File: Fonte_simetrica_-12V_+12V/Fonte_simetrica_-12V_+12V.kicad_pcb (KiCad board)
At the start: 2 copper layers, 23 parts, among them Q1 AO3401A, U1 TPS65131RGER

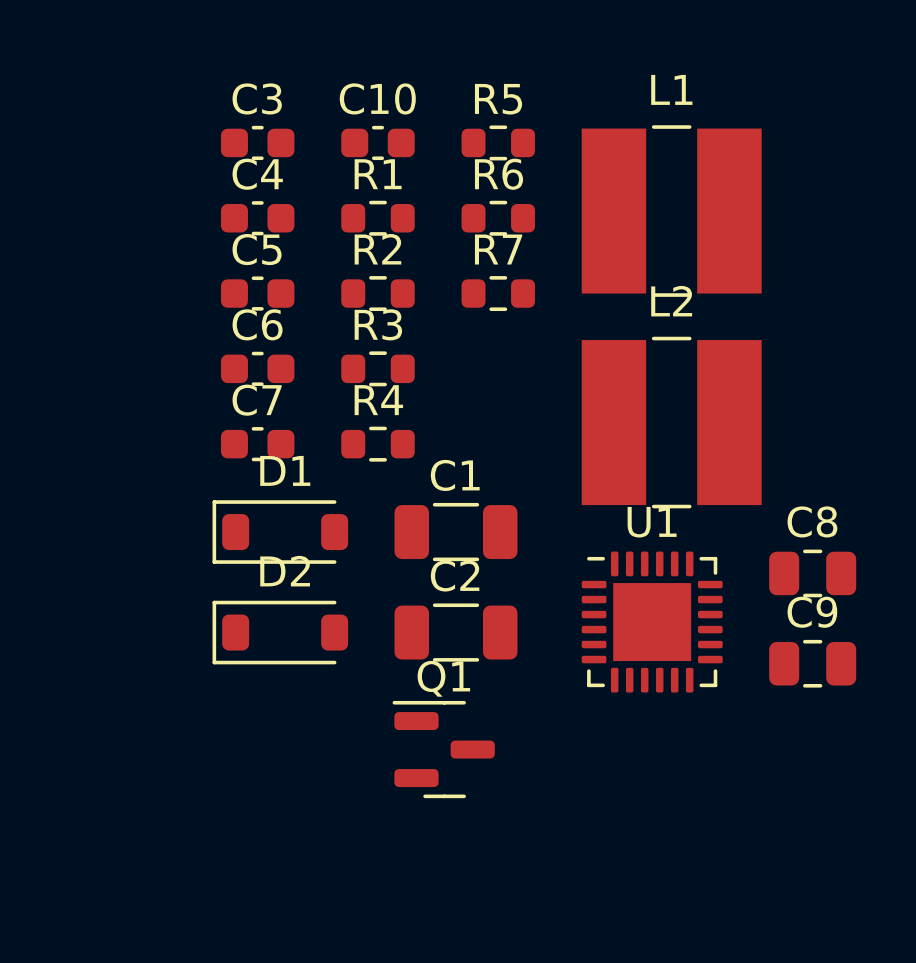
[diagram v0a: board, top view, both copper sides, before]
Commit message: add power 12+ and 12-
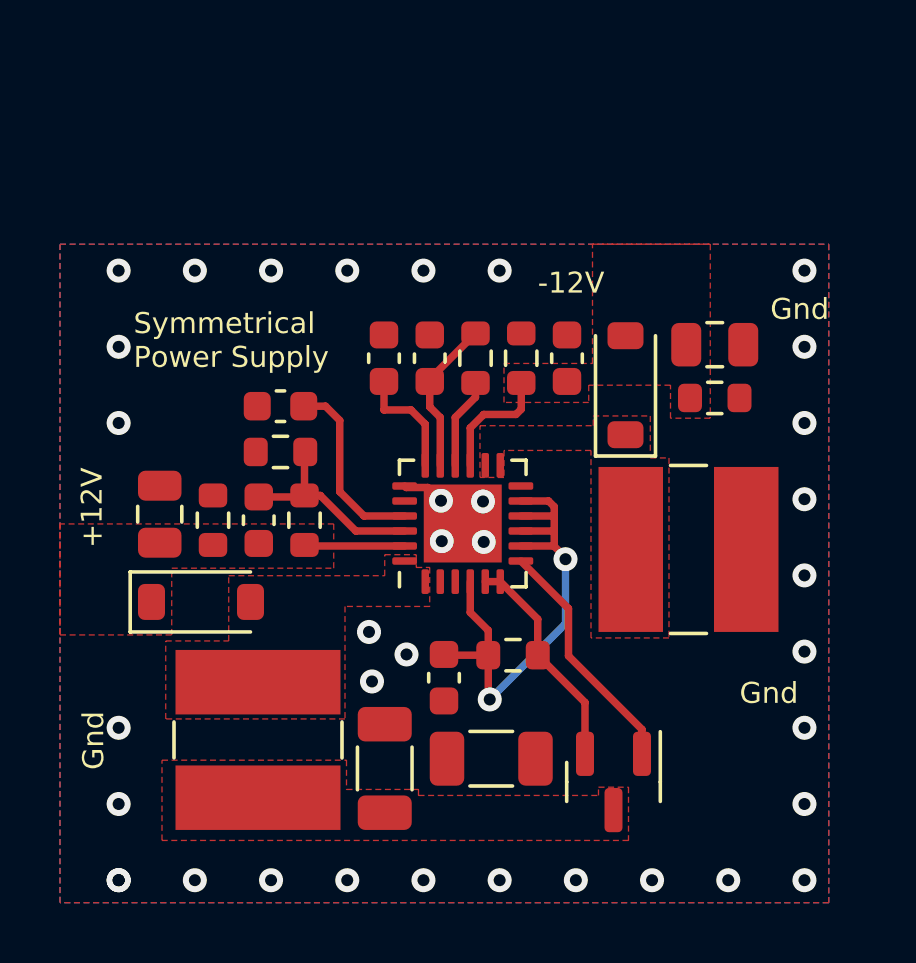
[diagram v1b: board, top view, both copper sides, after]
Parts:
- removed C1, C2: 10u, Capacitor_SMD:C_1206_3216Metric
- removed C10: 4n7, Capacitor_SMD:C_0603_1608Metric
- removed C3: 100n, Capacitor_SMD:C_0603_1608Metric
- removed C4: 10n, Capacitor_SMD:C_0603_1608Metric
- removed C5: 6p8, Capacitor_SMD:C_0603_1608Metric
- removed C6: 8p2, Capacitor_SMD:C_0603_1608Metric
- removed C7: 220n, Capacitor_SMD:C_0603_1608Metric
- removed C8, C9: 22u, Capacitor_SMD:C_0805_2012Metric
- removed D1, D2: B5819W, Diode_SMD:D_SOD-123
- removed L1, L2: 10u, Inductor_SMD:L_TracoPower_TCK-047_5.2x5.8mm
- removed Q1: AO3401A, Package_TO_SOT_SMD:SOT-23
- removed R1: 100, Resistor_SMD:R_0603_1608Metric
- removed R2, R5: 1M, Resistor_SMD:R_0603_1608Metric
- removed R3: 110k, Resistor_SMD:R_0603_1608Metric
- removed R4: 100k, Resistor_SMD:R_0603_1608Metric
- removed R6, R7: 12k, Resistor_SMD:R_0603_1608Metric
- removed U1: TPS65131RGER, Package_DFN_QFN:QFN-24-1EP_4x4mm_P0.5mm_EP2.6x2.6mm
- added CFS1: 10u, Capacitor_SMD:C_1206_3216Metric, F.Cu at (142.1, 82.0)
- added CFS10: 4n7, Capacitor_SMD:C_0603_1608Metric, F.Cu at (138.6, 68.6)
- added CFS2: 10u, Capacitor_SMD:C_1206_3216Metric, F.Cu at (138.6, 82.3)
- added CFS3: 100n, Capacitor_SMD:C_0603_1608Metric, F.Cu at (140.6, 79.3)
- added CFS4: 10n, Capacitor_SMD:C_0603_1608Metric, F.Cu at (135.1, 70.2)
- added CFS5: 6p8, Capacitor_SMD:C_0603_1608Metric, F.Cu at (134.4, 74.0)
- added CFS6: 8p2, Capacitor_SMD:C_0603_1608Metric, F.Cu at (144.7, 68.6)
- added CFS7: 220n, Capacitor_SMD:C_0603_1608Metric, F.Cu at (140.1, 68.6)
- added CFS8: 22u, Capacitor_SMD:C_0805_2012Metric, F.Cu at (149.6, 68.2)
- added CFS9: 22u, Capacitor_SMD:C_0805_2012Metric, F.Cu at (131.1, 73.8)
- added DFS1: B5819W, Diode_SMD:D_SOD-123, F.Cu at (132.4, 76.8)
- added DFS2: B5819W, Diode_SMD:D_SOD-123, F.Cu at (146.6, 69.5)
- added LFS1: 10u, Inductor_SMD:L_TracoPower_TCK-047_5.2x5.8mm, F.Cu at (134.3, 81.3)
- added LFS2: 10u, Inductor_SMD:L_TracoPower_TCK-047_5.2x5.8mm, F.Cu at (148.7, 75.0)
- added QFS1: AO3401A, Package_TO_SOT_SMD:SOT-23, F.Cu at (146.2, 82.8)
- added RFS1: 100, Resistor_SMD:R_0603_1608Metric, F.Cu at (142.8, 78.5)
- added RFS2: 1M, Resistor_SMD:R_0603_1608Metric, F.Cu at (135.9, 74.0)
- added RFS3: 110k, Resistor_SMD:R_0603_1608Metric, F.Cu at (135.1, 71.8)
- added RFS4: 100k, Resistor_SMD:R_0603_1608Metric, F.Cu at (141.6, 68.6)
- added RFS5: 1M, Resistor_SMD:R_0603_1608Metric, F.Cu at (143.1, 68.6)
- added RFS6: 12k, Resistor_SMD:R_0603_1608Metric, F.Cu at (149.6, 70.0)
- added RFS7: 12k, Resistor_SMD:R_0603_1608Metric, F.Cu at (132.8, 74.0)
- added UFS1: TPS65131RGER, Package_DFN_QFN:QFN-24-1EP_4x4mm_P0.5mm_EP2.6x2.6mm, F.Cu at (141.2, 74.1)
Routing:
- net Net-(UFS1-ENN): track 0.00 -> 17.8 mm, vias 0 -> 2
- net Net-(QFS1-G): track 0.00 -> 8.10 mm
- net +5V: track 0.00 -> 7.41 mm
- net Net-(UFS1-FBP): track 0.00 -> 6.83 mm
- net Net-(UFS1-CP): track 0.00 -> 6.27 mm
- net Net-(UFS1-VREF): track 0.00 -> 5.17 mm
- net -12V: track 0.00 -> 4.08 mm
- net Net-(UFS1-CN): track 0.00 -> 3.89 mm
- net +12L: track 0.00 -> 3.35 mm
- net Net-(UFS1-FBN): track 0.00 -> 3.03 mm
- net GND: track 0.00 -> 1.42 mm, vias 0 -> 36
- added copper zone on F.Cu, net +12L
- added copper zone on F.Cu, net -12V
- added copper zone on F.Cu, net /INP
- added copper zone on F.Cu, net /OUT
- added copper zone on F.Cu, net /n_mos
- added copper zone on B.Cu, net GND
- added copper zone on F.Cu, net GND
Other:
- board text added: "+12V"
- board text added: "-12V"
- board text added: "Gnd"
- board text added: "Symmetrical Power Supply"
